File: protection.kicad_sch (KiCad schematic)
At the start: 17 parts, among them Q301 FDS3672, U301 LM74700

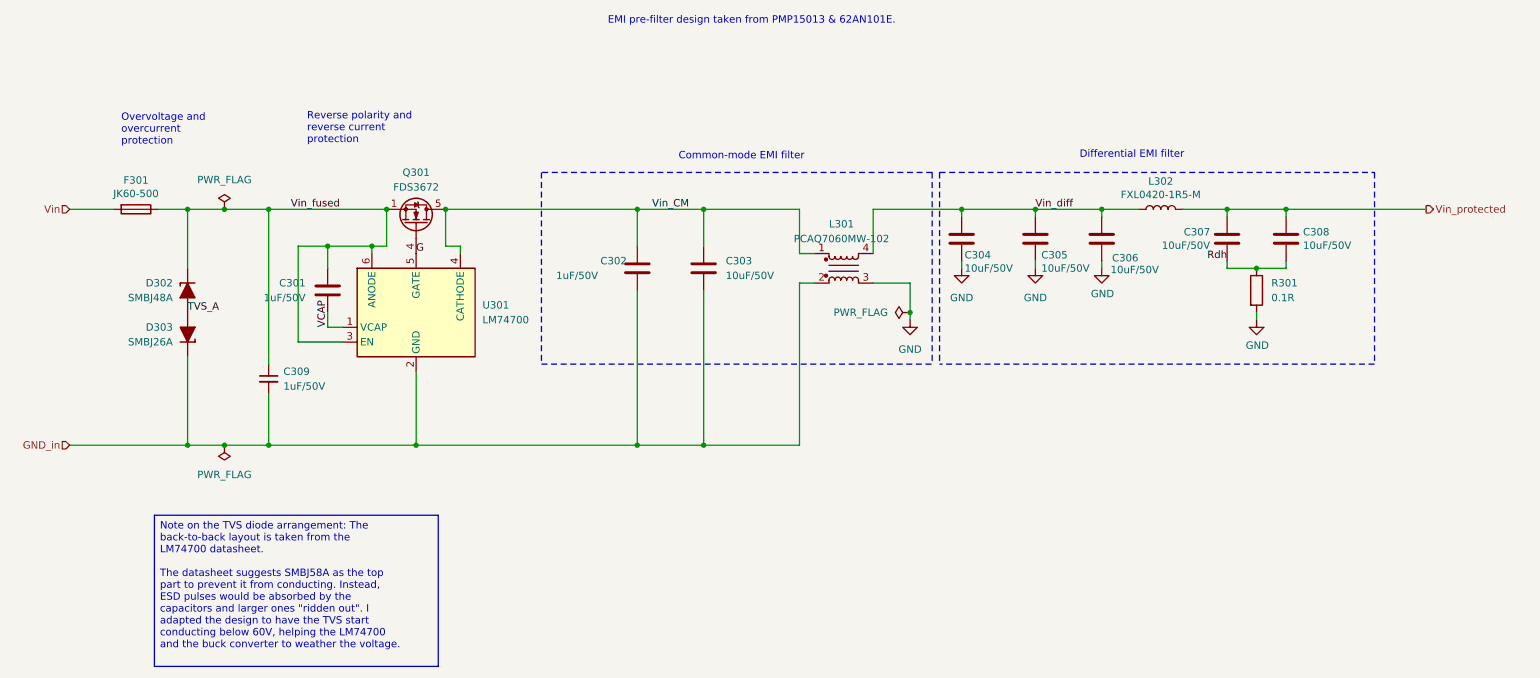
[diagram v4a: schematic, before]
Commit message: Finish the board redesign with SoM on the bottom
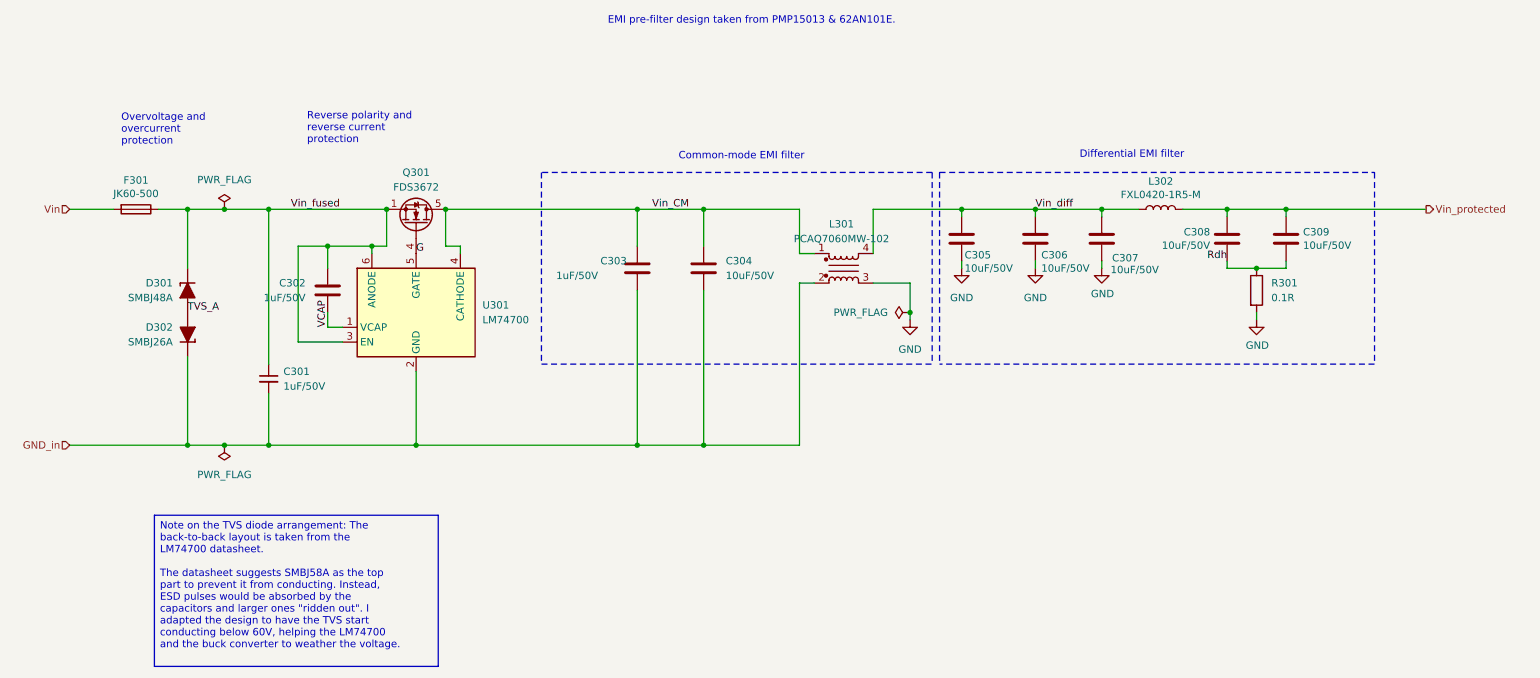
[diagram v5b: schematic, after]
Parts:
- D301: renamed from D302; footprint Diode_SMD:D_SMB -> PCM_Diode_SMD_AKL:D_SMB
- D302: renamed from D303; footprint Diode_SMD:D_SMB -> PCM_Diode_SMD_AKL:D_SMB
- F301: footprint Hatlabs:Polyfuse_JK60-500 -> Hatlabs:FUSE-TH_L24.1-W3.0-P10.20-D1.2-S2.0
- renumbered C309 to C301, C301 to C302, C302 to C303, C303 to C304, C304 to C305, C305 to C306, C306 to C307, C307 to C308, C308 to C309
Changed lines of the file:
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@@
 			)
 		)
-		(property "Footprint" "Hatlabs:Polyfuse_JK60-500"
+		(property "Footprint" "Hatlabs:FUSE-TH_L24.1-W3.0-P10.20-D1.2-S2.0"
 			(at 43.18 51.562 90)
 			(effects
@@
 			)
 		)
-		(property "Description" ""
+		(property "Description" "Fuse"
 			(at 43.18 53.34 0)
 			(effects
@@
 		(on_board yes)
 		(dnp no)
-		(property "Reference" "C306"
+		(property "Reference" "C307"
 			(at 211.328 61.722 0)
 			(effects
@@
 			)
 		)
-		(property "Description" ""
+		(property "Description" "Unpolarized capacitor"
 			(at 209.55 58.42 0)
 			(effects
@@
 			(project "SH-RPi"
 				(path "/abc482bd-3f17-4d35-80db-1da3dcdb5c27/c7bf4e1f-6bd1-4be7-9e56-1bd438bf5d42/b9ac802e-51d9-4be8-a7d3-5b5fa2c8bb97"
-					(reference "C306")
+					(reference "C307")
 					(unit 1)
 				)
@@
 			)
 		)
-		(property "Description" ""
+		(property "Description" "Inductor"
 			(at 219.71 53.34 0)
 			(effects
@@
 		(on_board yes)
 		(dnp no)
-		(property "Reference" "C307"
+		(property "Reference" "C308"
 			(at 228.219 57.2516 0)
 			(effects
@@
 			)
 		)
-		(property "Description" ""
+		(property "Description" "Unpolarized capacitor"
 			(at 231.14 58.42 0)
 			(effects
@@
 			(project "SH-RPi"
 				(path "/abc482bd-3f17-4d35-80db-1da3dcdb5c27/c7bf4e1f-6bd1-4be7-9e56-1bd438bf5d42/b9ac802e-51d9-4be8-a7d3-5b5fa2c8bb97"
-					(reference "C307")
+					(reference "C308")
 					(unit 1)
 				)
@@
 		(on_board yes)
 		(dnp no)
-		(property "Reference" "D302"
+		(property "Reference" "D301"
 			(at 49.53 66.0399 90)
 			(effects
@@
 			)
 		)
-		(property "Footprint" "Diode_SMD:D_SMB"
+		(property "Footprint" "PCM_Diode_SMD_AKL:D_SMB"
 			(at 52.07 67.31 0)
 			(effects
@@
 			)
 		)
-		(property "Description" "SMB Unidirectional TVS diode, 48V, 600W, Alternate KiCAD Library"
+		(property "Description" "SMB Unidirectional TVS diode, 58V, 600W, Alternate KiCAD Library"
 			(at 52.07 67.31 0)
 			(effects
@@
 			(project ""
 				(path "/abc482bd-3f17-4d35-80db-1da3dcdb5c27/c7bf4e1f-6bd1-4be7-9e56-1bd438bf5d42/b9ac802e-51d9-4be8-a7d3-5b5fa2c8bb97"
-					(reference "D302")
+					(reference "D301")
 					(unit 1)
 				)
@@
 			)
 		)
-		(property "Description" ""
+		(property "Description" "Resistor"
 			(at 236.22 67.31 0)
 			(effects
@@
 		(on_board yes)
 		(dnp no)
-		(property "Reference" "D303"
+		(property "Reference" "D302"
 			(at 49.53 73.6599 90)
 			(effects
@@
 			)
 		)
-		(property "Footprint" "Diode_SMD:D_SMB"
+		(property "Footprint" "PCM_Diode_SMD_AKL:D_SMB"
 			(at 52.07 74.93 0)
 			(effects
@@
 			(project ""
 				(path "/abc482bd-3f17-4d35-80db-1da3dcdb5c27/c7bf4e1f-6bd1-4be7-9e56-1bd438bf5d42/b9ac802e-51d9-4be8-a7d3-5b5fa2c8bb97"
-					(reference "D303")
+					(reference "D302")
 					(unit 1)
 				)
@@
 		(dnp no)
 		(fields_autoplaced yes)
-		(property "Reference" "C309"
+		(property "Reference" "C301"
 			(at 68.58 81.2862 0)
 			(effects
@@
 			(project ""
 				(path "/abc482bd-3f17-4d35-80db-1da3dcdb5c27/c7bf4e1f-6bd1-4be7-9e56-1bd438bf5d42/b9ac802e-51d9-4be8-a7d3-5b5fa2c8bb97"
-					(reference "C309")
+					(reference "C301")
 					(unit 1)
 				)
@@
 		(on_board yes)
 		(dnp no)
-		(property "Reference" "C308"
+		(property "Reference" "C309"
 			(at 244.221 57.2516 0)
 			(effects
@@
 			)
 		)
-		(property "Description" ""
+		(property "Description" "Unpolarized capacitor"
 			(at 241.3 58.42 0)
 			(effects
@@
 			(project "Yellow"
 				(path "/abc482bd-3f17-4d35-80db-1da3dcdb5c27/c7bf4e1f-6bd1-4be7-9e56-1bd438bf5d42/b9ac802e-51d9-4be8-a7d3-5b5fa2c8bb97"
-					(reference "C308")
+					(reference "C309")
 					(unit 1)
 				)
@@
 		(dnp no)
 		(fields_autoplaced yes)
-		(property "Reference" "C303"
+		(property "Reference" "C304"
 			(at 144.78 62.2299 0)
 			(effects
@@
 			)
 		)
-		(property "Description" ""
+		(property "Description" "Unpolarized capacitor"
 			(at 140.97 63.5 0)
 			(effects
@@
 			(project "SH-RPi"
 				(path "/abc482bd-3f17-4d35-80db-1da3dcdb5c27/c7bf4e1f-6bd1-4be7-9e56-1bd438bf5d42/b9ac802e-51d9-4be8-a7d3-5b5fa2c8bb97"
-					(reference "C303")
+					(reference "C304")
 					(unit 1)
 				)
@@
 		(on_board yes)
 		(dnp no)
-		(property "Reference" "C304"
+		(property "Reference" "C305"
 			(at 185.928 61.214 0)
 			(effects
@@
 			)
 		)
-		(property "Description" ""
+		(property "Description" "Unpolarized capacitor"
 			(at 185.42 58.42 0)
 			(effects
@@
 			(project "Yellow"
 				(path "/abc482bd-3f17-4d35-80db-1da3dcdb5c27/c7bf4e1f-6bd1-4be7-9e56-1bd438bf5d42/b9ac802e-51d9-4be8-a7d3-5b5fa2c8bb97"
-					(reference "C304")
+					(reference "C305")
 					(unit 1)
 				)
@@
 		(on_board yes)
 		(dnp no)
-		(property "Reference" "C305"
+		(property "Reference" "C306"
 			(at 199.136 61.214 0)
 			(effects
@@
 			)
 		)
-		(property "Description" ""
+		(property "Description" "Unpolarized capacitor"
 			(at 198.12 58.42 0)
 			(effects
@@
 			(project "SH-RPi"
 				(path "/abc482bd-3f17-4d35-80db-1da3dcdb5c27/c7bf4e1f-6bd1-4be7-9e56-1bd438bf5d42/b9ac802e-51d9-4be8-a7d3-5b5fa2c8bb97"
-					(reference "C305")
+					(reference "C306")
 					(unit 1)
 				)
@@
 		(on_board yes)
 		(dnp no)
-		(property "Reference" "C302"
+		(property "Reference" "C303"
 			(at 123.19 62.23 0)
 			(effects
@@
 			)
 		)
-		(property "Description" ""
+		(property "Description" "Unpolarized capacitor"
 			(at 129.54 63.5 0)
 			(effects
@@
 			(project "SH-RPi"
 				(path "/abc482bd-3f17-4d35-80db-1da3dcdb5c27/c7bf4e1f-6bd1-4be7-9e56-1bd438bf5d42/b9ac802e-51d9-4be8-a7d3-5b5fa2c8bb97"
-					(reference "C302")
+					(reference "C303")
 					(unit 1)
 				)
@@
 			)
 		)
-		(property "Datasheet" "https://www.lcsc.com/datasheet/lcsc_datasheet_2209231500_PROD-Tech-PCAQ7060MW-102_C2915648.pdf"
+		(property "Datasheet" "~"
 			(at 165.1 63.5 0)
 			(effects
@@
 			)
 		)
-		(property "Description" ""
+		(property "Description" "Coupled inductor with iron core"
 			(at 165.1 63.5 0)
 			(effects
@@
 		(on_board yes)
 		(dnp no)
-		(property "Reference" "C301"
+		(property "Reference" "C302"
 			(at 72.39 66.0399 0)
 			(effects
@@
 			)
 		)
-		(property "Description" ""
+		(property "Description" "Unpolarized capacitor"
 			(at 76.2 67.31 0)
 			(effects
@@
 			(project "HALPI2"
 				(path "/abc482bd-3f17-4d35-80db-1da3dcdb5c27/c7bf4e1f-6bd1-4be7-9e56-1bd438bf5d42/b9ac802e-51d9-4be8-a7d3-5b5fa2c8bb97"
-					(reference "C301")
-					(unit 1)
-				)
+					(reference "C302")
+					(unit 1)
+				)

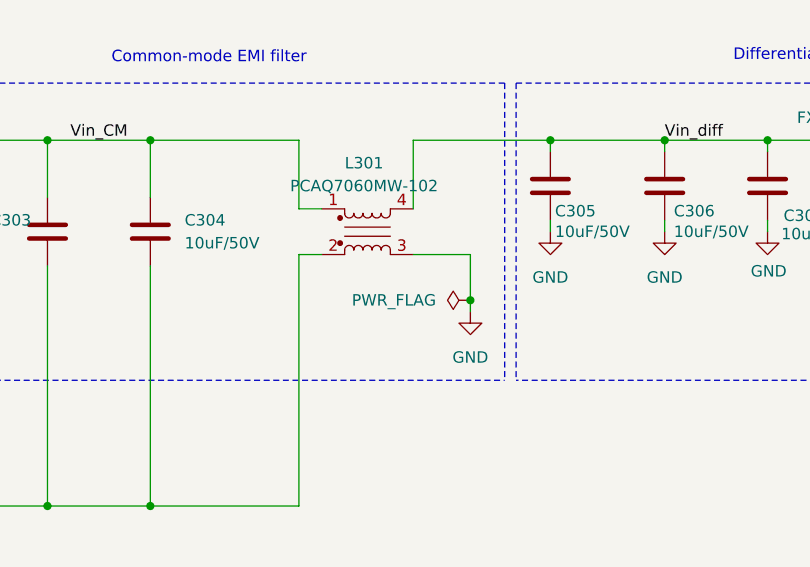
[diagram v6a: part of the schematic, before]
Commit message: Finish transitioning to RP2040
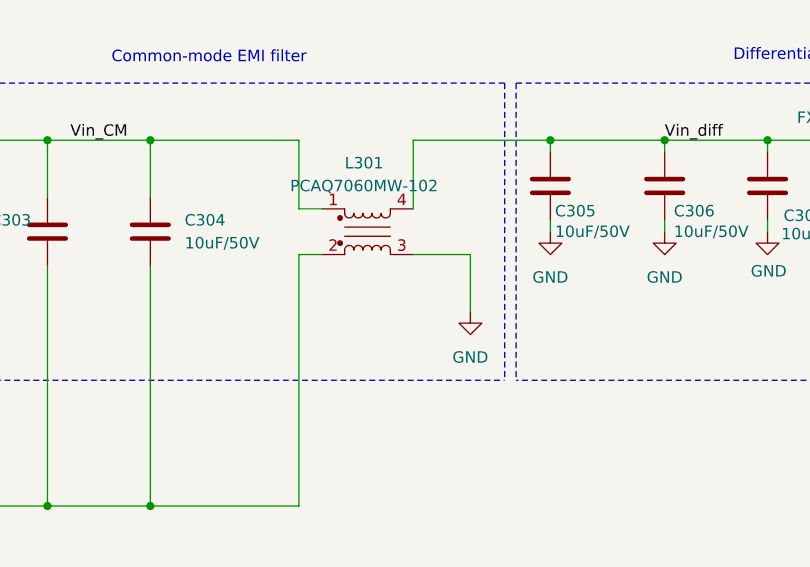
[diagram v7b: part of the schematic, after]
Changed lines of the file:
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@@
-	)
-	(junction
-		(at 176.53 71.12)
-		(diameter 0)
-		(color 0 0 0 0)
 	)
 	(junction
@@
 	(wire
 		(pts
-			(xy 176.53 66.04) (xy 176.53 71.12)
-		)
-		(stroke
-			(width 0)
-			(type default)
-		)
-	)
-	(wire
-		(pts
-			(xy 176.53 72.39) (xy 176.53 71.12)
+			(xy 176.53 66.04) (xy 176.53 72.39)
 		)
 		(stroke
@@
 					(unit 1)
 				)
-			)
-		)
-	)
-	(symbol
-		(lib_id "power:PWR_FLAG")
-		(at 176.53 71.12 90)
-		(unit 1)
-		(exclude_from_sim no)
-		(in_bom yes)
-		(on_board yes)
-		(dnp no)
-		(fields_autoplaced yes)
-		(property "Reference" "#FLG0303"
-			(at 174.625 71.12 0)
-			(effects
-				(font
-					(size 1.27 1.27)
-				)
-				(hide yes)
-			)
-		)
-		(property "Value" "PWR_FLAG"
-			(at 172.72 71.1199 90)
-			(effects
-				(font
-					(size 1.27 1.27)
-				)
-				(justify left)
-			)
-		)
-		(property "Footprint" ""
-			(at 176.53 71.12 0)
-			(effects
-				(font
-					(size 1.27 1.27)
-				)
-				(hide yes)
-			)
-		)
-		(property "Datasheet" "~"
-			(at 176.53 71.12 0)
-			(effects
-				(font
-					(size 1.27 1.27)
-				)
-				(hide yes)
-			)
-		)
-		(property "Description" "Special symbol for telling ERC where power comes from"
-			(at 176.53 71.12 0)
-			(effects
-				(font
-					(size 1.27 1.27)
-				)
-				(hide yes)
-			)
-		)
-		(pin "1"
-		)
-		(instances
-			(project "HALPI2"
-				(path "/abc482bd-3f17-4d35-80db-1da3dcdb5c27/c7bf4e1f-6bd1-4be7-9e56-1bd438bf5d42/b9ac802e-51d9-4be8-a7d3-5b5fa2c8bb97"
-					(reference "#FLG0303")
-					(unit 1)
-				)

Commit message: Apply part PCBA position corrections
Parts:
- Q301, U301: JLCPCB_CORRECTION (none) -> 0;0;270
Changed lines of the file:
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@@
+			)
+		)
+		(property "JLCPCB_CORRECTION" "0;0;270"
+			(at 91.44 71.12 0)
+			(effects
+				(font
+					(size 1.27 1.27)
+				)
+				(hide yes)
 			)
 		)
@@
 			)
 		)
-		(property "LCSC Part" ""
-			(at 91.44 55.88 0)
-			(effects
-				(font
-					(size 1.27 1.27)
-				)
-			)
-		)
 		(property "Sim.Enable" ""
 			(at 91.44 55.88 0)
@@
 			)
 		)
+		(property "JLCPCB_CORRECTION" "0;0;270"
+			(at 91.44 55.88 0)
+			(effects
+				(font
+					(size 1.27 1.27)
+				)
+				(hide yes)
+			)
+		)
